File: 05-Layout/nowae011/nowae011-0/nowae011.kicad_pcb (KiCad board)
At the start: 2 copper layers, 22.9 x 10.2 mm, 15 parts, among them P1 VIN, P2 VOUT, U1 ST1S14PHR

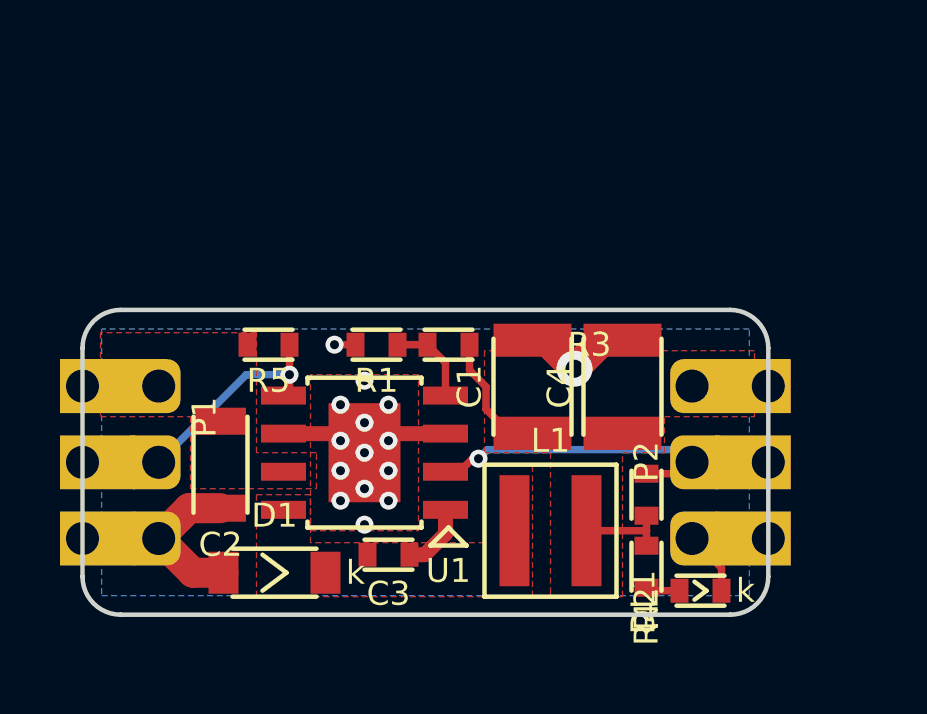
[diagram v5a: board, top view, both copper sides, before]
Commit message: WiP: placement silkscreen (nowae011-0)
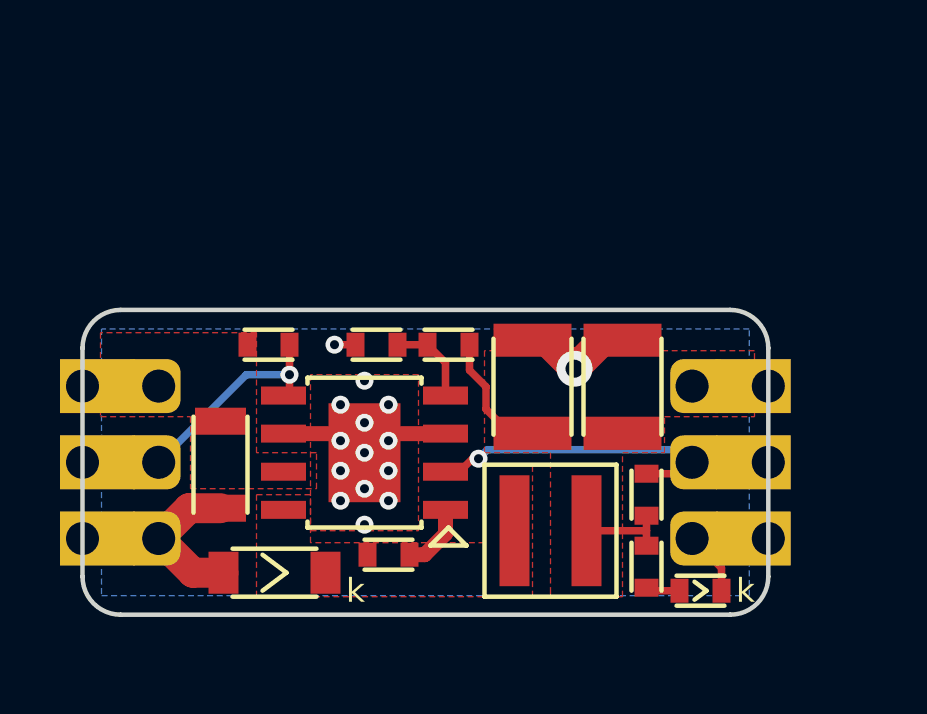
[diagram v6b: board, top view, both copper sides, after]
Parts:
- added G***: LOGO, LOGO:LOGO_NOWAE_10MM_FSILK, B.Cu at (15.7, -5.08)
- added G***: LOGO, EXTLOGO:LOGO_OSH_5MM_FSILK, B.Cu at (8.64, -6.60)
- added G***: LOGO, EXTLOGO:LOGO_CC-BY-SA_5MM_FSILK, B.Cu at (8.64, -2.03)
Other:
- board text added: "+24VIN"
- board text added: "+VOUT"
- board text added: "EN"
- board text added: "GND"
- board text added: "NOWAE011-0"
- board text added: "PG"

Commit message: Fixed silkscreen top (nowae011-0)
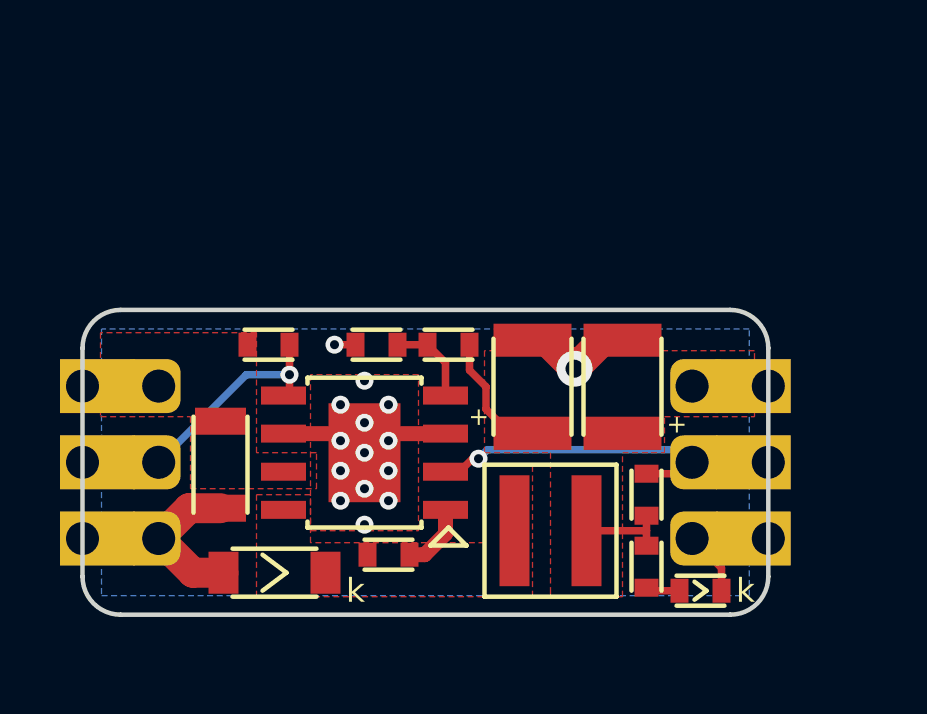
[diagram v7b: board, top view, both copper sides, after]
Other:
- board text added: "+"
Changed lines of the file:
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@@
   (general
     (thickness 1.6)
-    (drawings 17)
+    (drawings 19)
     (tracks 67)
     (zones 0)
@@
     (35 F.Paste user hide)
     (36 B.SilkS user)
-    (37 F.SilkS user hide)
+    (37 F.SilkS user)
     (38 B.Mask user)
     (39 F.Mask user hide)
@@
     (trace_clearance 0.2)
     (zone_clearance 0.381)
-    (zone_45_only no)
+    (zone_45_only yes)
     (trace_min 0.2)
     (segment_width 0.2)
@@
       (xy 1.205726 0.879611) (xy 1.289793 0.879612) (xy 1.369962 0.879611)) (layer B.SilkS) (width 0.01))
   )
+  (gr_text + (at 19.812 -6.35) (layer F.SilkS)
+    (effects (font (size 0.6 0.6) (thickness 0.15)))
+  )
+  (gr_text + (at 13.208 -6.604) (layer F.SilkS)
+    (effects (font (size 0.6 0.6) (thickness 0.15)))
+  )
   (gr_text NOWAE011-0 (at 13.462 -5.08 270) (layer B.SilkS)
